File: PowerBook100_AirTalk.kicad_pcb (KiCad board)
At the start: 2 copper layers, 41 parts, among them J1 5-104652-2, J2 PRG_HDR, Q1 BSS138, SW1 RST, U1 TashTalk, U2 TXB0104PWR, U3 AMS1117-3.3, U4 ESP32-WROOM-32DM113DH6400PH3Q0, U5 74LVC2G125

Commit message: More mods
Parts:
- removed TP1: RX_PB, TestPoint:TestPoint_Pad_2.0x2.0mm
- removed TP2: TX_PB, TestPoint:TestPoint_Pad_2.0x2.0mm
- removed TP3: RTS_PB, TestPoint:TestPoint_Pad_2.0x2.0mm
- added R12: R, Resistor_SMD:R_0805_2012Metric, F.Cu at (38.7, 17.3)
- added R17: 0, Resistor_SMD:R_0805_2012Metric, F.Cu at (1.71, 0.97)
- added R18: 0, Resistor_SMD:R_0805_2012Metric, F.Cu at (1.71, 3.92)
- added R19: 0, Resistor_SMD:R_0805_2012Metric, F.Cu at (1.71, 6.88)
- C1: footprint Capacitor_SMD:CP_Elec_4x5.8 -> Capacitor_SMD:C_1206_3216Metric
- C11, C2, C3, C4, C5, C7: footprint Capacitor_SMD:CP_Elec_6.3x7.7 -> Capacitor_SMD:C_1206_3216Metric
- J2: footprint Connector_Samtec_HPM_THT:Samtec_HPM-03-01-x-S_Straight_1x03_Pitch5.08mm -> Connector_PinHeader_2.00mm:PinHeader_1x03_P2.00mm_Vertical_SMD_Pin1Right; moved to B.Cu
- U1: footprint Package_DIP:DIP-8_W7.62mm -> Package_SO:SOIC-8-1EP_3.9x4.9mm_P1.27mm_EP2.29x3mm; moved to B.Cu
- U3: footprint Package_TO_SOT_SMD:SOT-223-3_TabPin2 -> Package_TO_SOT_SMD:TO-252-3_TabPin2
- U4: moved to B.Cu
- moved SW1 153.0 mm to (4.40, 29.9)
- moved J2 115.7 mm to (4.83, 31.1), turned to 90 degrees
- moved J1 93.6 mm to (78.3, 16.2), turned to -90 degrees
- moved U4 91.4 mm to (7.71, 16.8), turned to -90 degrees
- moved C4 83.5 mm to (30.4, 64.6)
- moved D2 83.5 mm to (64.6, 95.0)
- moved C1 83.5 mm to (30.4, 40.2)
- moved C11 83.5 mm to (30.4, 89.1)
- moved C2 83.5 mm to (30.4, 48.3)
- moved C3 83.5 mm to (30.4, 56.5)
- moved C9 83.5 mm to (50.3, 86.2)
- moved R10 83.5 mm to (63.5, 83.1)
- moved R11 83.5 mm to (63.5, 86.0)
- moved R14 83.5 mm to (67.9, 83.1)
- moved R15 83.5 mm to (67.9, 86.0)
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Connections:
- J1 pad 14: unconnected-(J1-Pad14) -> PB_CTS
- J1 pad 18: unconnected-(J1-Pad18) -> /MODEM_5v
- J1 pad 20: unconnected-(J1-Pad20) -> /MODEM_5v
- J1 pad 5: +5V -> /ALWAYS_ON_5V
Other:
- board outline added: 81.8 x 33.5 mm

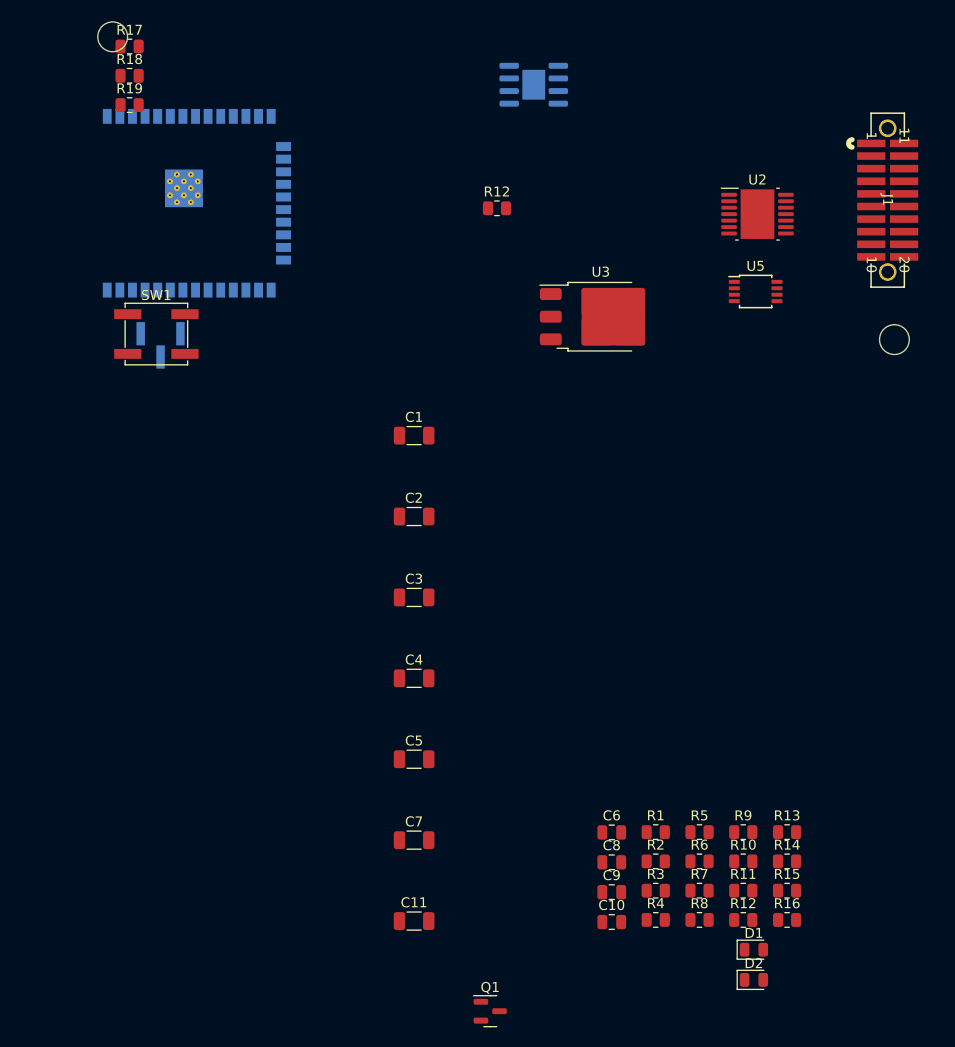
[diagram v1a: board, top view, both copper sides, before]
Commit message: Add PCB layout
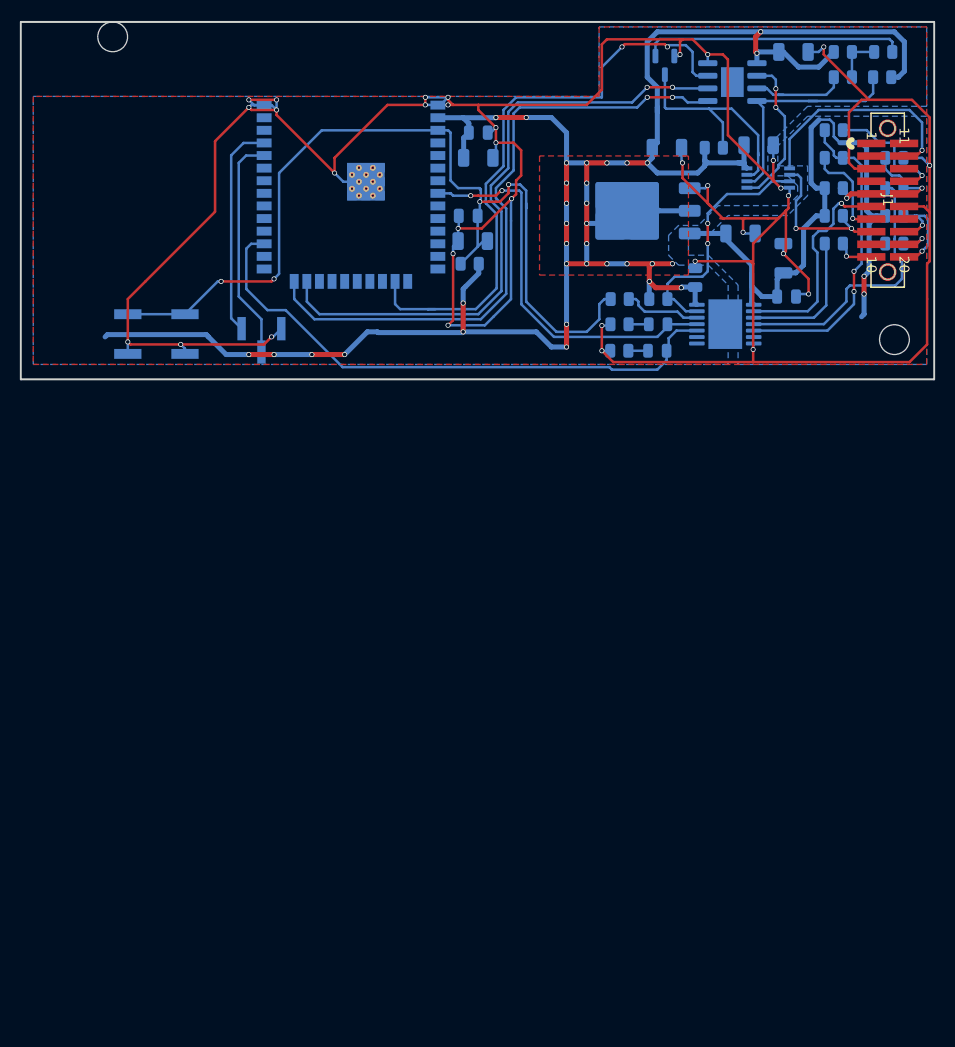
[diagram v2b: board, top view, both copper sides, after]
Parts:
- removed the R12 at (63.5, 89.0)
- removed the R12 at (38.7, 17.3)
- added R12: R, Resistor_SMD:R_0805_2012Metric, B.Cu at (55.0, 26.4)
- C1, C10, C11, C2, C3, C4, C5, C6, C7, C8, C9, D1, D2, Q1, R1, R10, R11, R13, R14, R15, R16, R17, R18, R19, R2, R3, R4, R5, R6, R7, R8, R9, SW1, U2, U3, U5: moved to B.Cu
- moved Q1 96.9 mm to (55.6, 2.87), turned to -90 degrees
- moved R8 86.1 mm to (73.6, 4.06), turned to 180 degrees
- moved R1 81.9 mm to (77.6, 1.52), turned to 180 degrees
- moved R6 81.1 mm to (77.5, 4.06)
- moved R9 79.2 mm to (73.6, 1.52)
- moved R17 78.9 mm to (78.7, 18.0), turned to 180 degrees
- moved C8 74.7 mm to (36.8, 9.65), turned to 180 degrees
- moved R11 74.4 mm to (72.6, 12.2)
- moved C4 73.8 mm to (68.6, 1.52)
- moved R4 72.2 mm to (78.7, 20.8), turned to 180 degrees
- moved R2 72.1 mm to (60.6, 11.2)
- moved R18 71.8 mm to (72.6, 15.2), turned to 180 degrees
- moved R19 71.0 mm to (72.6, 9.40), turned to 180 degrees
- moved C5 70.9 mm to (65.1, 10.9)
- moved R7 69.3 mm to (72.6, 18.0), turned to 180 degrees
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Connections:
- C5 pad 2: unconnected-(C5-Pad2) -> GND
- C8 pad 2: unconnected-(C8-Pad2) -> +3.3V
- R4 pad 2: unconnected-(R4-Pad2) -> Net-(U2-A3)
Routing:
- net GND: track 0.00 -> 354.3 mm, vias 0 -> 34
- net +3.3V: track 0.00 -> 216.1 mm, vias 0 -> 33
- net ESP_EN: track 0.00 -> 94.0 mm, vias 0 -> 4
- net +5V: track 0.00 -> 65.9 mm, vias 0 -> 2
- net ESP_CTS: track 0.00 -> 64.9 mm, vias 0 -> 2
- net ESP_TX: track 0.00 -> 63.5 mm, vias 0 -> 2
- net ESP_RX: track 0.00 -> 61.3 mm, vias 0 -> 2
- net GEN_ACTIVITY: track 0.00 -> 57.6 mm
- net WIFI_GREEN: track 0.00 -> 39.8 mm, vias 0 -> 2
- net Net-(U2-A4): track 0.00 -> 31.6 mm, vias 0 -> 2
- net Net-(U2-A3): track 0.00 -> 29.1 mm
- net Net-(Q1-G): track 0.00 -> 26.5 mm
- net LT_TX_33: track 0.00 -> 25.8 mm, vias 0 -> 2
- net Net-(U1-LT_IN): track 0.00 -> 24.1 mm
- net Net-(Q1-D): track 0.00 -> 23.5 mm
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- added copper zone on B.Cu, net +3.3V
- added copper zone on F.Cu, net +3.3V
- added copper zone on B.Cu, net +5V
- added copper zone on F.Cu, net GND
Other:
- board size 81.8 x 33.5 mm -> 92 x 36 mm

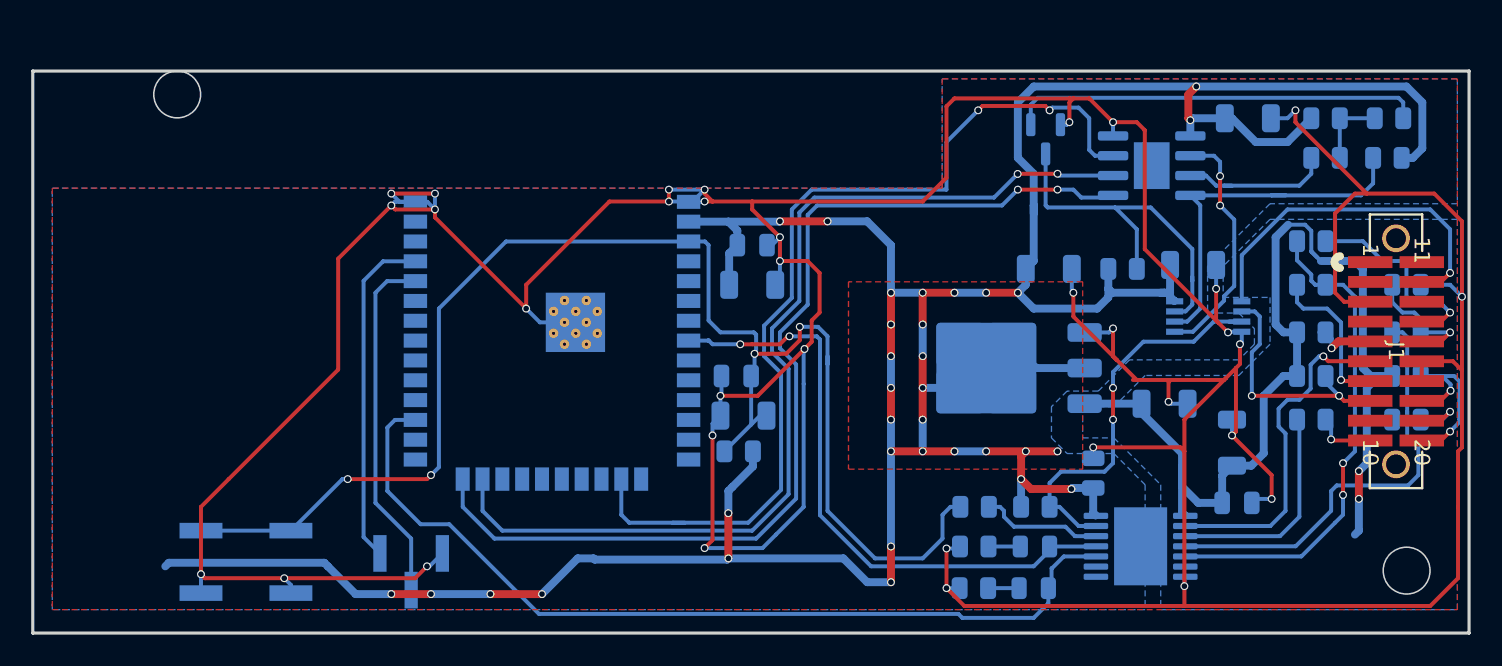
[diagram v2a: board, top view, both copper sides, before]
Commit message: Add proper dimensions
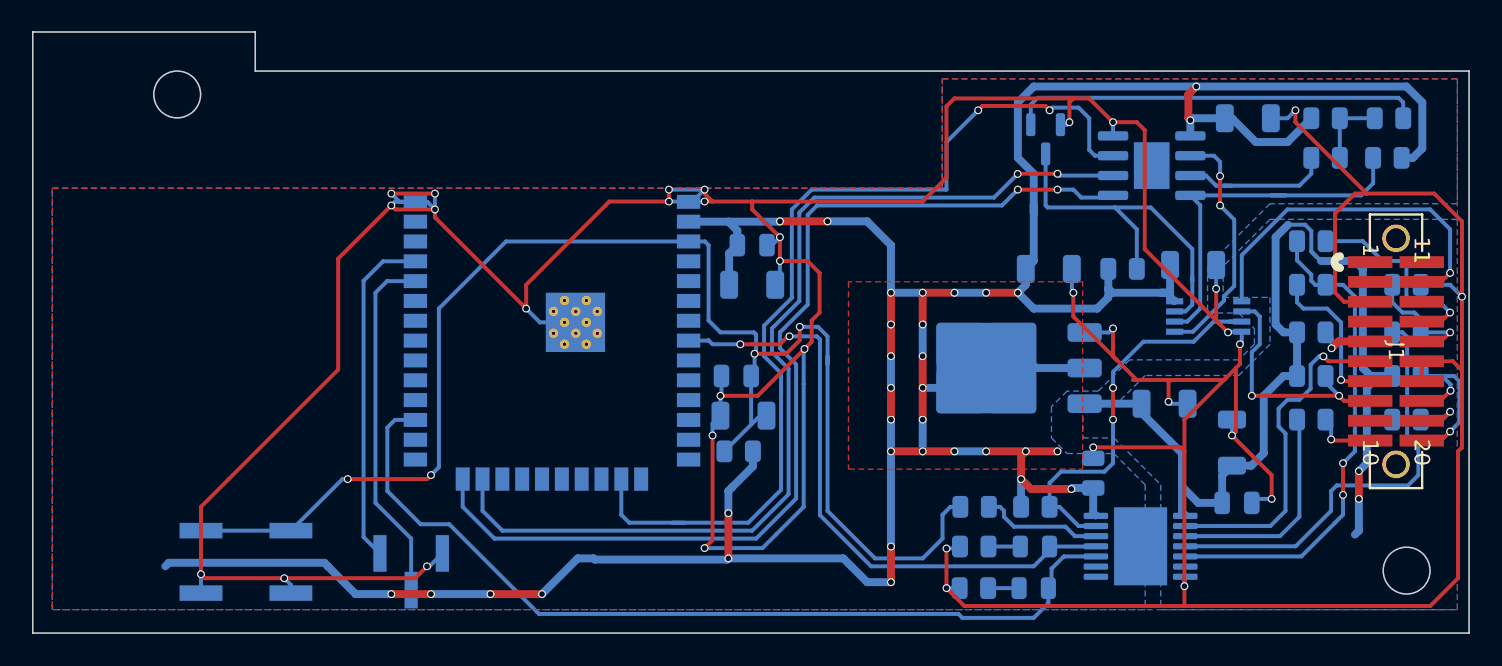
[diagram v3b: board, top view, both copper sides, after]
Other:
- board size 92 x 36 mm -> 92 x 38.5 mm
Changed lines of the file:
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@@
     )
   )
+  (gr_line (start 82.75 34.5) (end -9.25 34.5)
+    (stroke (width 0.1) (type default)) (layer "Edge.Cuts"))
+  (gr_line (start 5 -4) (end 5 -1.5)
+    (stroke (width 0.1) (type default)) (layer "Edge.Cuts"))
+  (gr_line (start -9.25 34.5) (end -9.25 -4)
+    (stroke (width 0.1) (type default)) (layer "Edge.Cuts"))
+  (gr_line (start 82.75 -1.5) (end 82.75 34.5)
+    (stroke (width 0.1) (type default)) (layer "Edge.Cuts"))
+  (gr_line (start -9.25 -4) (end 5 -4)
+    (stroke (width 0.1) (type default)) (layer "Edge.Cuts"))
   (gr_circle locked (center 78.75 30.5) (end 80.25 30.5)
     (stroke (width 0.1) (type default)) (fill none) (layer "Edge.Cuts"))
-  (gr_rect (start -9.25 -1.5) (end 82.75 34.5)
-    (stroke (width 0.2) (type default)) (fill none) (layer "Edge.Cuts"))
+  (gr_line (start 5 -1.5) (end 82.75 -1.5)
+    (stroke (width 0.1) (type default)) (layer "Edge.Cuts"))
   (gr_circle locked (center 0 0) (end 1.5 0)
     (stroke (width 0.1) (type default)) (fill none) (layer "Edge.Cuts"))

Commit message: New revision
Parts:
- removed C3: 22u, Capacitor_SMD:C_1206_3216Metric
- removed R1: 470, Resistor_SMD:R_0805_2012Metric
- removed R13, R14, R17, R18, R19: 0, Resistor_SMD:R_0805_2012Metric
- removed U2: TXB0104PWR, Package_SO:HTSSOP-14-1EP_4.4x5mm_P0.65mm_EP3.4x5mm_Mask3x3.1mm
- added C12: 0.1uF, Capacitor_SMD:C_1206_3216Metric, B.Cu at (-0.64, 20.2)
- added D3: 3.3V, LED_SMD:LED_0805_2012Metric, B.Cu at (44.6, 30.6)
- added D4: 5V, LED_SMD:LED_0805_2012Metric, B.Cu at (66.2, 21.0)
- added R20: 10K, Resistor_SMD:R_0805_2012Metric, B.Cu at (11.4, 23.5)
- added R21: 10K, Resistor_SMD:R_0805_2012Metric, B.Cu at (71.6, 12.5)
- added SW2: TS-1187A-B-A-B, Button_Switch_SMD:SW_Push_1P1T_XKB_TS-1187A, B.Cu at (5.60, 20.3)
- added U6: TXU0304PWR, footprints:TSSOP14_PW_TEX, B.Cu at (63.3, 27.3)
- C1: value 22u -> 10uF; footprint Capacitor_SMD:C_1206_3216Metric -> Capacitor_SMD:C_0805_2012Metric
- C10, C9: value 1uF -> 0.1uF
- C2: value 1000u -> 22uF; footprint Capacitor_SMD:C_1206_3216Metric -> Capacitor_SMD:C_0805_2012Metric
- C6, C8: value 0.1u -> 0.1uF
- C7: value 22u -> 22uF
- J2: value PRG_HDR -> PRG; footprint Connector_PinHeader_2.00mm:PinHeader_1x03_P2.00mm_Vertical_SMD_Pin1Right -> Connector_PinHeader_1.00mm:PinHeader_1x04_P1.00mm_Vertical_SMD_Pin1Right
- R10, R12: value R -> 10K
- R3: value 0 -> 470
- R4: value 0 -> 10K
- R5: value 0 -> 1K
- SW1: value RST -> TS-1187A-B-A-B; footprint Button_Switch_SMD:SW_SPST_EVPBF -> Button_Switch_SMD:SW_Push_1P1T_XKB_TS-1187A
- U1: footprint Package_SO:SOIC-8-1EP_3.9x4.9mm_P1.27mm_EP2.29x3mm -> Package_SO:SOIC-8_3.9x4.9mm_P1.27mm
- moved C11 38.2 mm to (-0.80, 29.8), turned to -90 degrees
- moved R3 33.4 mm to (40.7, 30.7), turned to 0 degrees
- moved R12 23.8 mm to (70.0, 8.00), turned to 90 degrees
- moved R6 20.2 mm to (58.7, 11.2)
- moved R11 18.8 mm to (57.5, 23.2), turned to 90 degrees
- moved C4 12.3 mm to (56.2, 1.25)
- moved R8 11.8 mm to (62.5, 8.15)
- moved R9 11.8 mm to (62.5, 5.61)
- moved D1 11.0 mm to (44.6, 25.2)
- moved R15 11.0 mm to (40.7, 25.2)
- moved R16 11.0 mm to (40.7, 28.0)
- moved D2 10.9 mm to (44.6, 27.9)
- moved R2 10.6 mm to (66.7, 2.50), turned to -90 degrees
- moved R5 10.4 mm to (70.1, 21.0), turned to 180 degrees
- moved Q1 7.14 mm to (62.7, 1.89)
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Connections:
- C11 pad 1: GND -> Net-(C11-Pad1)
- C11 pad 2: ESP_EN -> Net-(C11-Pad2)
- C2 pad 1: +5V -> +3.3V
- J1 pad 11: unconnected-(J1-Pad11) -> GND
- J1 pad 15: MODEM_INSERT -> /MODEM_INS
- J1 pad 18: /MODEM_5v -> +5V
- J1 pad 2: unconnected-(J1-Pad2) -> /MODEM_PWR
- J1 pad 20: /MODEM_5v -> +5V
- J1 pad 5: /ALWAYS_ON_5V -> unconnected-(J1-Pad5)
- J2 pad 1: GND -> Net-(J2-Pin_1)
- J2 pad 3: Net-(J2-Pin_3) -> GND
- R11 pad 1: RING_DT -> Net-(U6-A4Y)
- R11 pad 2: Net-(U2-A4) -> ESP_EN
- R3 pad 1: DTR_PB -> GND
- R4 pad 1: /DCD -> /MODEM_INS
- R4 pad 2: Net-(U2-A3) -> GND
- R5 pad 1: Net-(U2-A3) -> GND
- R5 pad 2: MODEM_INSERT -> Net-(D4-K)
- R8 pad 1: Net-(R1-Pad2) -> Net-(Q1-G)
- R9 pad 2: Net-(R1-Pad2) -> Net-(Q1-G)
- SW1 pad 1: ESP_EN -> Net-(C11-Pad2)
- SW1 pad 2: GND -> ESP_EN
- U4 pad 15: unconnected-(U4-GND-Pad15) -> GND
- U4 pad 35: Net-(J2-Pin_3) -> Net-(J2-Pin_1)
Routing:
- net GND: track 354.3 -> 290.7 mm, vias 34 -> 5
- net Net-(U2-A4): track 31.6 -> 0.00 mm, vias 2 -> 0
- net Net-(U2-A3): track 29.1 -> 0.00 mm
- net Net-(J2-Pin_3): track 21.7 -> 0.00 mm
- net Net-(J2-Pin_1): track 0.00 -> 20.7 mm
- net ESP_TX: track 63.5 -> 42.9 mm
- net ESP_EN: track 94.0 -> 74.6 mm, vias 4 -> 2
- net ESP_RX: track 61.3 -> 42.2 mm, vias 2 -> 0
- net Net-(Q1-G): track 26.5 -> 7.89 mm
- net ESP_CTS: track 64.9 -> 46.6 mm
- net /MODEM_5v: track 13.5 -> 0.00 mm, vias 2 -> 0
- net DTR_PB: track 3.95 -> 17.0 mm
- net /RTS_PB: track 22.9 -> 9.82 mm
- net +5V: track 65.9 -> 53.0 mm, vias 2 -> 1
- net /DCD: track 4.50 -> 17.1 mm
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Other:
- board text added: "."
- board text added: "PowerBook AirTalk RZ 2023"
- board text added: "PowerBook Airtalk Modem Adapter RZ 2023"
- board text added: "RST"
- board text added: "SETUP"
